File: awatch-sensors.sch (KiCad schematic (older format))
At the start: 0 parts

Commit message: add sensors
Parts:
- added C? (x2): 1µF, symbol Device:C_Small
- added C? (x6): .1µF, symbol Device:C_Small
- added R? (x15): 0, symbol Device:R_Small_US
- added R? (x2): 2.2k, symbol Device:R_Small_US
- added R? (x2): n/c, symbol Device:R_Small_US
- added U?: APDS-9306-065, symbol awatch-parts:APDS-9306-065
- added U?: BMI160, symbol awatch-parts:BMI160
- added U?: BMM150, symbol awatch-parts:BMM150
- added U?: BMP388, symbol awatch-parts:BMP388
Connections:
- new net: R?.1, U?.1 (SCL)
- new net: R?.1, U?.2 (SDA)
- new net: R?.2, U?.1 (SDO)
- new net: R?.1, U?.12 (CSB)
- new net: R?.2, U?.13 (SCx)
- new net: R?.2, U?.14 (SDx)
- new net: R?.1, R?.2, U?.2 (ASDx)
- new net: R?.1, R?.2, U?.3 (ASCx)
- new net: R?.1, R?.2, U?.B4 (SDI)
- new net: R?.1, R?.2, U?.A3 (SCK)
- new net: R?.1, U?.A1 (PS)
- new net: R?.2, U?.A5 (CSB)
- new net: R?.2, U?.C1 (SDO)
- new net: R?.1, U?.2 (SCK)
- new net: R?.1, U?.4 (SDI)
- new net: R?.2, U?.5 (SDO)
- new net: R?.1, U?.6 (CSB)
- new net +2V8: C?.1, C?.1, C?.1, C?.1, C?.1, C?.1, C?.1, C?.1, R?.1, R?.1, R?.2, R?.2, R?.2, U?.1 (VDDIO), U?.10 (VDD), U?.3 (VDD), U?.5 (VDDIO), U?.8 (VDD), U?.B2 (VDDIO), U?.E5 (VDD)
- new net GND: C?.2, C?.2, C?.2, C?.2, C?.2, C?.2, C?.2, C?.2, R?.1, R?.1, R?.1, R?.1, U?.6 (GND), U?.6 (GNDIO), U?.7 (GND), U?.8 (GND), U?.9 (GND), U?.C5 (GND), U?.E1 (GND), U?.E3 (GND)
- new net SENS_IMU_INT: U?.4 (INT1)
- new net SENS_SCL: R?.1, R?.2, R?.2, R?.2
- new net SENS_SDA: R?.1, R?.2, R?.2, R?.2
- no-connect marks 0 -> 7
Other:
- note added: "ALS I2C address 7’h52"
- note added: "Baro I2C address 7’h76"
- note added: "IMU I2C address 7’h68"
- note added: "Mag I2C address 7’h10"
- note added: "NOTE:\ncould save a few uW by putting sensor\nVDD on different rail from VDDIO\n(sensors can tolerate 1.8V)"
- note added: "place near\nVDD/GND"
- note added: "place near\nVDDIO/GNDIO"

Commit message: annotate all
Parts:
- gave numbers to parts that had none: 31

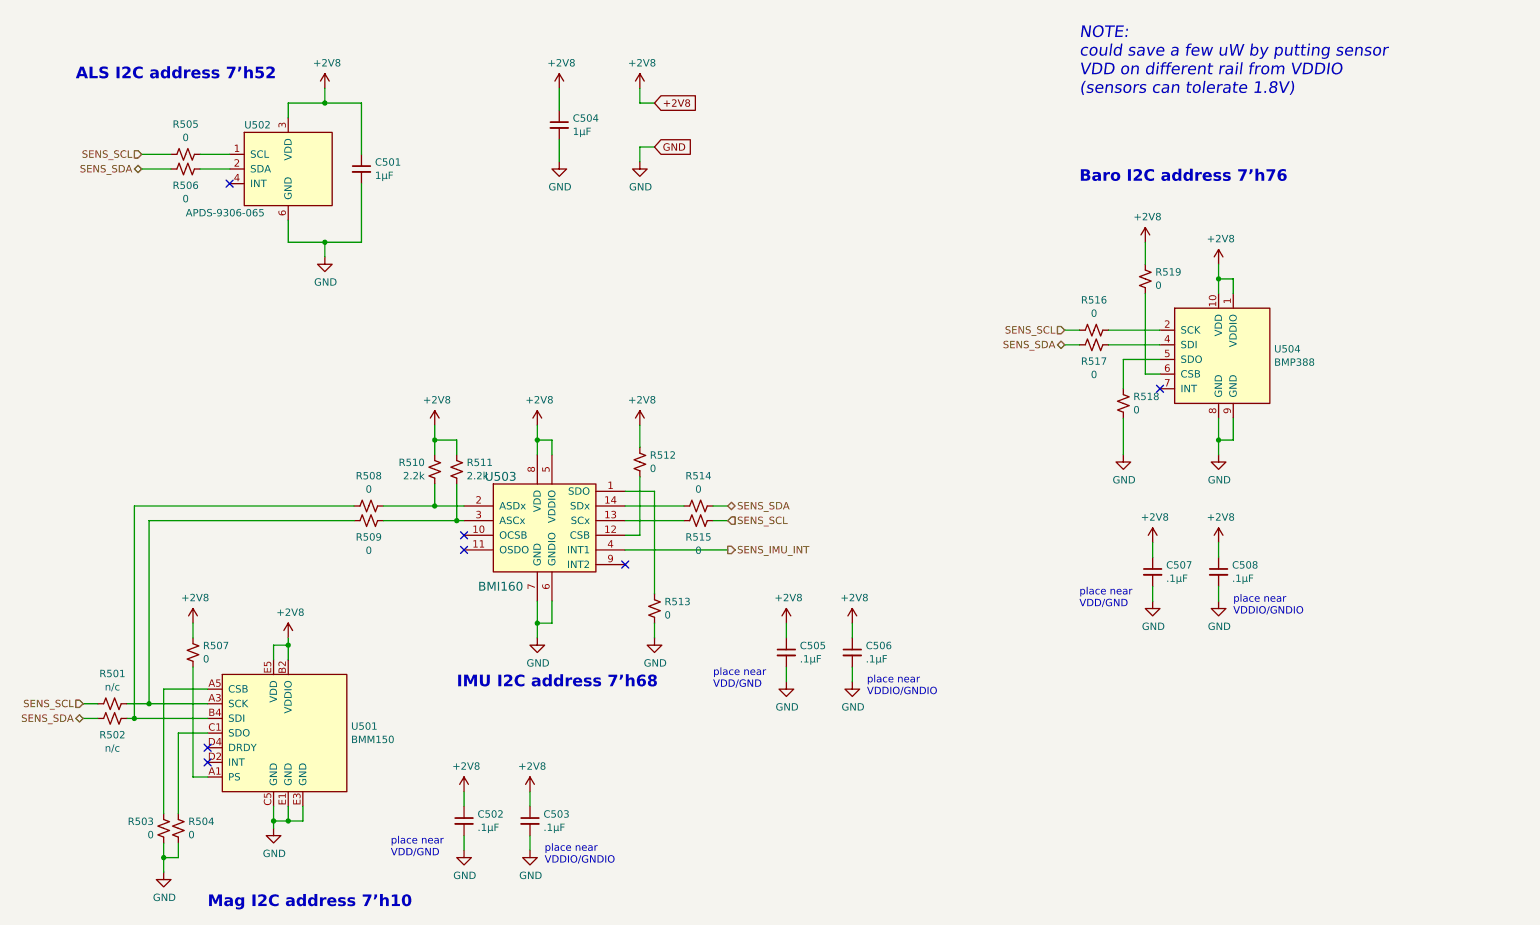
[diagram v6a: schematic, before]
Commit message: add power measurement cuts
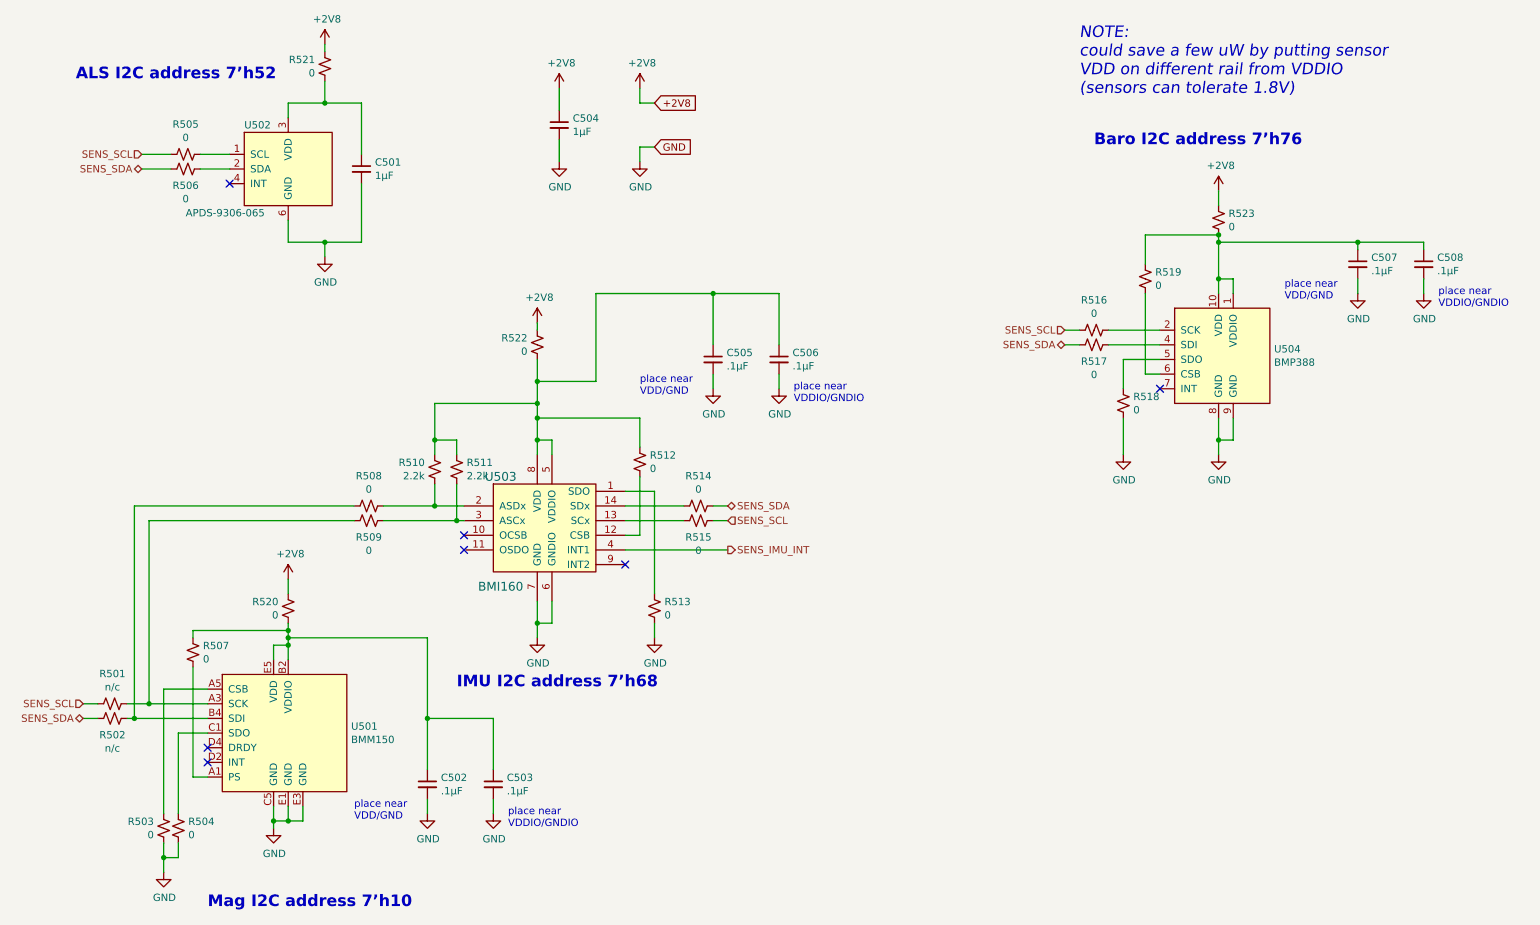
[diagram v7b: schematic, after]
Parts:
- added R520, R521, R522, R523: 0, symbol Device:R_Small_US
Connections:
- net +2V8: now also R520.2, R521.2, R522.2, R523.2; no longer C501.1, C502.1, C503.1, C505.1, C506.1, C507.1, C508.1, R507.2, R510.1, R511.1, R512.2, R519.2, U501.B2 (VDDIO), U501.E5 (VDD), U502.3 (VDD), U503.5 (VDDIO), U503.8 (VDD), U504.1 (VDDIO), U504.10 (VDD)
- new net: C501.1, R521.1, U502.3 (VDD)
- new net: C505.1, C506.1, R510.1, R511.1, R512.2, R522.1, U503.5 (VDDIO), U503.8 (VDD)
- new net: C502.1, C503.1, R507.2, R520.1, U501.B2 (VDDIO), U501.E5 (VDD)
- new net: C507.1, C508.1, R519.2, R523.1, U504.1 (VDDIO), U504.10 (VDD)
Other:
- moved on the sheet: C502, C503, C505, C506, C507, C508

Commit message: Add footprints.
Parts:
- C501, C502, C503, C504, C505, C506, C507, C508: footprint (none) -> Capacitor_SMD:C_0603_1608Metric
- R501, R502, R503, R504, R505, R506, R507, R508, R509, R510, R511, R512, R513, R514, R515, R516, R517, R518, R519, R520, R521, R522, R523: footprint (none) -> Resistor_SMD:R_0603_1608Metric
- U501: footprint (none) -> awatch2-footprints:WLCSP-12_1.56x1.56mm_Layout5x5_P0.283mm_Ball0.25mm_Pad0.2mm_NSMD
- U502: footprint (none) -> awatch2-footprints:DFN-6_2x2mm_P0.53mm
- U503: footprint (none) -> awatch2-footprints:BMI160
- U504: footprint (none) -> awatch2-footprints:BMP388
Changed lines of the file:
@@
 EESchema Schematic File Version 4
+LIBS:awatch2-cache
 EELAYER 26 0
 EELAYER END
@@
 F 0 "U502" H 2300 1650 50  0000 L CNN
 F 1 "APDS-9306-065" H 1900 1050 50  0000 L CNN
-F 2 "" H 2200 1650 50  0001 C CNN
+F 2 "awatch2-footprints:DFN-6_2x2mm_P0.53mm" H 2200 1650 50  0001 C CNN
 F 3 "" H 2200 1650 50  0001 C CNN
 	1    2200 1650
@@
 F 0 "R505" V 1695 1850 50  0000 C CNN
 F 1 "0" V 1786 1850 50  0000 C CNN
-F 2 "" H 1900 1850 50  0001 C CNN
+F 2 "Resistor_SMD:R_0603_1608Metric" H 1900 1850 50  0001 C CNN
 F 3 "~" H 1900 1850 50  0001 C CNN
 	1    1900 1850
@@
 F 0 "R506" V 2013 1950 50  0000 C CNN
 F 1 "0" V 2104 1950 50  0000 C CNN
-F 2 "" H 1900 1950 50  0001 C CNN
+F 2 "Resistor_SMD:R_0603_1608Metric" H 1900 1950 50  0001 C CNN
 F 3 "~" H 1900 1950 50  0001 C CNN
 	1    1900 1950
@@
 F 0 "C501" H 3192 1996 50  0000 L CNN
 F 1 "1µF" H 3192 1905 50  0000 L CNN
-F 2 "" H 3100 1950 50  0001 C CNN
+F 2 "Capacitor_SMD:C_0603_1608Metric" H 3100 1950 50  0001 C CNN
 F 3 "~" H 3100 1950 50  0001 C CNN
 	1    3100 1950
@@
 F 0 "U503" H 4050 4750 60  0000 C CNN
 F 1 "BMI160" H 4050 4000 60  0000 C CNN
-F 2 "" H 4050 4650 60  0001 C CNN
+F 2 "awatch2-footprints:BMI160" H 4050 4650 60  0001 C CNN
 F 3 "" H 4050 4650 60  0001 C CNN
 	1    4350 4400
@@
 F 0 "R512" H 4932 3904 50  0000 R CNN
 F 1 "0" H 4932 3995 50  0000 R CNN
-F 2 "" H 5000 3950 50  0001 C CNN
+F 2 "Resistor_SMD:R_0603_1608Metric" H 5000 3950 50  0001 C CNN
 F 3 "~" H 5000 3950 50  0001 C CNN
 	1    5000 3950
@@
 F 0 "R513" H 5032 4904 50  0000 R CNN
 F 1 "0" H 5032 4995 50  0000 R CNN
-F 2 "" H 5100 4950 50  0001 C CNN
+F 2 "Resistor_SMD:R_0603_1608Metric" H 5100 4950 50  0001 C CNN
 F 3 "~" H 5100 4950 50  0001 C CNN
 	1    5100 4950
@@
 F 0 "R515" V 5513 4350 50  0000 C CNN
 F 1 "0" V 5604 4350 50  0000 C CNN
-F 2 "" H 5400 4350 50  0001 C CNN
+F 2 "Resistor_SMD:R_0603_1608Metric" H 5400 4350 50  0001 C CNN
 F 3 "~" H 5400 4350 50  0001 C CNN
 	1    5400 4350
@@
 F 0 "R514" V 5195 4250 50  0000 C CNN
 F 1 "0" V 5286 4250 50  0000 C CNN
-F 2 "" H 5400 4250 50  0001 C CNN
+F 2 "Resistor_SMD:R_0603_1608Metric" H 5400 4250 50  0001 C CNN
 F 3 "~" H 5400 4250 50  0001 C CNN
 	1    5400 4250
@@
 F 0 "R508" V 2945 4250 50  0000 C CNN
 F 1 "0" V 3036 4250 50  0000 C CNN
-F 2 "" H 3150 4250 50  0001 C CNN
+F 2 "Resistor_SMD:R_0603_1608Metric" H 3150 4250 50  0001 C CNN
 F 3 "~" H 3150 4250 50  0001 C CNN
 	1    3150 4250
@@
 F 0 "R509" V 3263 4350 50  0000 C CNN
 F 1 "0" V 3354 4350 50  0000 C CNN
-F 2 "" H 3150 4350 50  0001 C CNN
+F 2 "Resistor_SMD:R_0603_1608Metric" H 3150 4350 50  0001 C CNN
 F 3 "~" H 3150 4350 50  0001 C CNN
 	1    3150 4350
@@
 F 0 "R510" H 3532 4046 50  0000 R CNN
 F 1 "2.2k" H 3532 3955 50  0000 R CNN
-F 2 "" H 3600 4000 50  0001 C CNN
+F 2 "Resistor_SMD:R_0603_1608Metric" H 3600 4000 50  0001 C CNN
 F 3 "~" H 3600 4000 50  0001 C CNN
 	1    3600 4000
@@
 F 0 "R511" H 3818 4046 50  0000 L CNN
 F 1 "2.2k" H 3818 3955 50  0000 L CNN
-F 2 "" H 3750 4000 50  0001 C CNN
+F 2 "Resistor_SMD:R_0603_1608Metric" H 3750 4000 50  0001 C CNN
 F 3 "~" H 3750 4000 50  0001 C CNN
 	1    3750 4000
@@
 F 0 "C502" H 3642 6196 50  0000 L CNN
 F 1 ".1µF" H 3642 6105 50  0000 L CNN
-F 2 "" H 3550 6150 50  0001 C CNN
+F 2 "Capacitor_SMD:C_0603_1608Metric" H 3550 6150 50  0001 C CNN
 F 3 "~" H 3550 6150 50  0001 C CNN
 	1    3550 6150
@@
 F 0 "C503" H 4092 6196 50  0000 L CNN
 F 1 ".1µF" H 4092 6105 50  0000 L CNN
-F 2 "" H 4000 6150 50  0001 C CNN
+F 2 "Capacitor_SMD:C_0603_1608Metric" H 4000 6150 50  0001 C CNN
 F 3 "~" H 4000 6150 50  0001 C CNN
 	1    4000 6150
@@
 F 0 "U501" H 3029 4846 50  0000 L CNN
 F 1 "BMM150" H 3029 4755 50  0000 L CNN
-F 2 "" H 2050 5300 50  0001 C CNN
+F 2 "awatch2-footprints:WLCSP-12_1.56x1.56mm_Layout5x5_P0.283mm_Ball0.25mm_Pad0.2mm_NSMD" H 2050 5300 50  0001 C CNN
 F 3 "" H 2050 5300 50  0001 C CNN
 	1    2050 5300
@@
 F 0 "C505" H 5592 3296 50  0000 L CNN
 F 1 ".1µF" H 5592 3205 50  0000 L CNN
-F 2 "" H 5500 3250 50  0001 C CNN
+F 2 "Capacitor_SMD:C_0603_1608Metric" H 5500 3250 50  0001 C CNN
 F 3 "~" H 5500 3250 50  0001 C CNN
 	1    5500 3250
@@
 F 0 "C506" H 6042 3296 50  0000 L CNN
 F 1 ".1µF" H 6042 3205 50  0000 L CNN
-F 2 "" H 5950 3250 50  0001 C CNN
+F 2 "Capacitor_SMD:C_0603_1608Metric" H 5950 3250 50  0001 C CNN
 F 3 "~" H 5950 3250 50  0001 C CNN
 	1    5950 3250
@@
 F 0 "R502" V 1513 5700 50  0000 C CNN
 F 1 "n/c" V 1604 5700 50  0000 C CNN
-F 2 "" H 1400 5700 50  0001 C CNN
+F 2 "Resistor_SMD:R_0603_1608Metric" H 1400 5700 50  0001 C CNN
 F 3 "~" H 1400 5700 50  0001 C CNN
 	1    1400 5700
@@
 F 0 "R501" V 1195 5600 50  0000 C CNN
 F 1 "n/c" V 1286 5600 50  0000 C CNN
-F 2 "" H 1400 5600 50  0001 C CNN
+F 2 "Resistor_SMD:R_0603_1608Metric" H 1400 5600 50  0001 C CNN
 F 3 "~" H 1400 5600 50  0001 C CNN
 	1    1400 5600
@@
 F 0 "R503" H 1817 6404 50  0000 L CNN
 F 1 "0" H 1817 6495 50  0000 L CNN
-F 2 "" H 1750 6450 50  0001 C CNN
+F 2 "Resistor_SMD:R_0603_1608Metric" H 1750 6450 50  0001 C CNN
 F 3 "~" H 1750 6450 50  0001 C CNN
 	1    1750 6450
@@
 F 0 "R504" H 1782 6404 50  0000 R CNN
 F 1 "0" H 1782 6495 50  0000 R CNN
-F 2 "" H 1850 6450 50  0001 C CNN
+F 2 "Resistor_SMD:R_0603_1608Metric" H 1850 6450 50  0001 C CNN
 F 3 "~" H 1850 6450 50  0001 C CNN
 	1    1850 6450
@@
 F 0 "R507" H 1882 5204 50  0000 R CNN
 F 1 "0" H 1882 5295 50  0000 R CNN
-F 2 "" H 1950 5250 50  0001 C CNN
+F 2 "Resistor_SMD:R_0603_1608Metric" H 1950 5250 50  0001 C CNN
 F 3 "~" H 1950 5250 50  0001 C CNN
 	1    1950 5250
@@
 F 0 "U504" H 9329 2621 50  0000 L CNN
 F 1 "BMP388" H 9329 2530 50  0000 L CNN
-F 2 "" H 8550 2900 50  0001 C CNN
+F 2 "awatch2-footprints:BMP388" H 8550 2900 50  0001 C CNN
 F 3 "" H 8550 2900 50  0001 C CNN
 	1    8550 2900
@@
 F 0 "C507" H 9992 2646 50  0000 L CNN
 F 1 ".1µF" H 9992 2555 50  0000 L CNN
-F 2 "" H 9900 2600 50  0001 C CNN
+F 2 "Capacitor_SMD:C_0603_1608Metric" H 9900 2600 50  0001 C CNN
 F 3 "~" H 9900 2600 50  0001 C CNN
 	1    9900 2600
@@
 F 0 "C508" H 10442 2646 50  0000 L CNN
 F 1 ".1µF" H 10442 2555 50  0000 L CNN
-F 2 "" H 10350 2600 50  0001 C CNN
+F 2 "Capacitor_SMD:C_0603_1608Metric" H 10350 2600 50  0001 C CNN
 F 3 "~" H 10350 2600 50  0001 C CNN
 	1    10350 2600
@@
 F 0 "R519" H 8382 2654 50  0000 R CNN
 F 1 "0" H 8382 2745 50  0000 R CNN
-F 2 "" H 8450 2700 50  0001 C CNN
+F 2 "Resistor_SMD:R_0603_1608Metric" H 8450 2700 50  0001 C CNN
 F 3 "~" H 8450 2700 50  0001 C CNN
 	1    8450 2700
@@
 F 0 "R516" V 7895 3050 50  0000 C CNN
 F 1 "0" V 7986 3050 50  0000 C CNN
-F 2 "" H 8100 3050 50  0001 C CNN
+F 2 "Resistor_SMD:R_0603_1608Metric" H 8100 3050 50  0001 C CNN
 F 3 "~" H 8100 3050 50  0001 C CNN
 	1    8100 3050
@@
 F 0 "R517" V 8213 3150 50  0000 C CNN
 F 1 "0" V 8304 3150 50  0000 C CNN
-F 2 "" H 8100 3150 50  0001 C CNN
+F 2 "Resistor_SMD:R_0603_1608Metric" H 8100 3150 50  0001 C CNN
 F 3 "~" H 8100 3150 50  0001 C CNN
 	1    8100 3150
@@
 F 0 "R518" H 8232 3504 50  0000 R CNN
 F 1 "0" H 8232 3595 50  0000 R CNN
-F 2 "" H 8300 3550 50  0001 C CNN
+F 2 "Resistor_SMD:R_0603_1608Metric" H 8300 3550 50  0001 C CNN
 F 3 "~" H 8300 3550 50  0001 C CNN
 	1    8300 3550
@@
 F 0 "C504" H 4542 1696 50  0000 L CNN
 F 1 "1µF" H 4542 1605 50  0000 L CNN
-F 2 "" H 4450 1650 50  0001 C CNN
+F 2 "Capacitor_SMD:C_0603_1608Metric" H 4450 1650 50  0001 C CNN
 F 3 "~" H 4450 1650 50  0001 C CNN
 	1    4450 1650
@@
 F 0 "R521" H 2917 1204 50  0000 L CNN
 F 1 "0" H 2917 1295 50  0000 L CNN
-F 2 "" H 2850 1250 50  0001 C CNN
+F 2 "Resistor_SMD:R_0603_1608Metric" H 2850 1250 50  0001 C CNN
 F 3 "~" H 2850 1250 50  0001 C CNN
 	1    2850 1250
@@
 F 0 "R522" H 4367 3104 50  0000 L CNN
 F 1 "0" H 4367 3195 50  0000 L CNN
-F 2 "" H 4300 3150 50  0001 C CNN
+F 2 "Resistor_SMD:R_0603_1608Metric" H 4300 3150 50  0001 C CNN
 F 3 "~" H 4300 3150 50  0001 C CNN
 	1    4300 3150
@@
 F 0 "R520" H 2667 4904 50  0000 L CNN
 F 1 "0" H 2667 4995 50  0000 L CNN
-F 2 "" H 2600 4950 50  0001 C CNN
+F 2 "Resistor_SMD:R_0603_1608Metric" H 2600 4950 50  0001 C CNN
 F 3 "~" H 2600 4950 50  0001 C CNN
 	1    2600 4950
@@
 F 0 "R523" H 8882 2254 50  0000 R CNN
 F 1 "0" H 8882 2345 50  0000 R CNN
-F 2 "" H 8950 2300 50  0001 C CNN
+F 2 "Resistor_SMD:R_0603_1608Metric" H 8950 2300 50  0001 C CNN
 F 3 "~" H 8950 2300 50  0001 C CNN
 	1    8950 2300
